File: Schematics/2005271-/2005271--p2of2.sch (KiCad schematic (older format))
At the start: 0 parts

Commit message: Finished up the CAD drawings for 2005271- (AGC module A22).
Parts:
- added G301: Ground-chassis, symbol AGC_DSKY:Ground-chassis
- added J3: ConnectorA1-300, symbol AGC_DSKY:ConnectorA1-300
- added J4: ConnectorA1-400, symbol AGC_DSKY:ConnectorA1-400
- added U201, U203, U205, U209, U211, U213, U214, U216, U218, U221, U224, U225, U227, U229, U231, U233, U235, U237, U239, U243, U245, U246, U248, U250, U252, U256, U258: D3NOR-+4SW-0VDCA-B_C-E_F, symbol D3NOR-+4SW-0VDCA:D3NOR-+4SW-0VDCA-B_C-E_F
- added U202, U204, U206, U208, U210, U212, U215, U217, U219, U222, U223, U226, U228, U230, U232, U234, U236, U238, U240, U242, U244, U247, U249, U251, U253, U255, U257, U259: D3NOR-+4SW-0VDCA-B_C-DFE, symbol D3NOR-+4SW-0VDCA:D3NOR-+4SW-0VDCA-B_C-DFE
- added U207: D3NOR-FAP-0VDCA-expander-ABC-EDF, symbol D3NOR-FAP-0VDCA-expander:D3NOR-FAP-0VDCA-expander-ABC-EDF
- added U220, U241: D3NOR-FAP-0VDCA-expander-ABC-DEF, symbol D3NOR-FAP-0VDCA-expander:D3NOR-FAP-0VDCA-expander-ABC-DEF
- added U254: D3NOR-FAP-0VDCA-expander-BAC-DEF, symbol D3NOR-FAP-0VDCA-expander:D3NOR-FAP-0VDCA-expander-BAC-DEF
- added U260: D3NOR-+4SW-0VDCA-B_C-D_F, symbol D3NOR-+4SW-0VDCA:D3NOR-+4SW-0VDCA-B_C-D_F
- added X301, X302, X303, X304, X311, X312, X313, X314, X315, X316: Node2, symbol AGC_DSKY:Node2
- added X305, X306, X307, X308, X309, X310, X317, X318, X319, X320, X321, X322, X323: ArrowTwiddle, symbol AGC_DSKY:ArrowTwiddle
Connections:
- new net: J3.358, U225.8 (F)
- new net: G301.1, J4.401
- new net: U252.7 (E), X312.1
- new net: U250.7 (E), X311.1
- new net: U248.7 (E), X315.1
- new net: J3.328, U202.2 (C), U204.2 (C), U206.2 (C), U208.2 (C), U210.2 (C), U212.3 (B), U215.2 (C), U217.2 (C), U219.2 (C), U222.2 (C), U223.2 (C), U226.2 (C), U228.2 (C), U230.2 (C)
- new net: U239.7 (E), X313.1
- new net: J4.458, U256.7 (E), X319.1 (pwr)
- new net: J4.453, U253.6 (D)
- new net: J4.457, U255.6 (D)
- new net: J3.314, U206.7 (E)
- new net: U237.7 (E), X316.1
- new net: U235.7 (E), X314.1
- new net: J3.326, U210.7 (E)
- new net: J3.320, U209.8 (F), X309.1 (pwr)
- new net: J4.434, U246.7 (E), X317.1 (pwr)
- new net: J3.342, U212.6 (D), U215.6 (D), U217.6 (D), U219.6 (D), U222.6 (D), U223.6 (D)
- new net: J3.340, U217.7 (E)
- new net: J3.345, U219.7 (E)
- new net: U218.1 (J), U219.3 (B), U219.8 (F)
- new net: U219.9 (K), U220.6 (D)
- new net: U218.3 (B), U219.1 (J)
- new net: J3.334, U201.7 (E), U203.7 (E), U205.7 (E), U209.7 (E), U211.7 (E), U213.7 (E), U214.8 (F), U216.7 (E), U218.7 (E), U221.7 (E), U224.7 (E), U225.7 (E), U227.8 (F), U229.7 (E)
- new net: J3.344, U218.8 (F), X307.1 (pwr)
- new net: U218.2 (C), U218.9 (K)
- new net: J3.330, U212.7 (E)
- new net: J3.337, U216.8 (F), X308.1 (pwr)
- new net: J3.335, U215.7 (E)
- new net: J4.440, U249.6 (D)
- new net: J3.331, U207.1 (J), U207.9 (K), U220.1 (J), U220.9 (K)
- new net: J4.469, U260.6 (D)
- new net: J4.437, U231.7 (E), U233.8 (F), U235.8 (F), U237.8 (F), U239.8 (F), U243.8 (F), U245.8 (F), U246.8 (F), U248.8 (F), U250.8 (F), U252.8 (F), U256.8 (F), U258.8 (F), U260.8 (F)
- new net: U260.2 (C), U260.9 (K)
- new net: U259.3 (B), U259.8 (F), U260.1 (J)
- new net: U259.1 (J), U260.3 (B)
- new net: J4.445, U251.6 (D)
- new net: J3.304, U202.6 (D)
- new net: J4.463, U258.7 (E)
- new net: U258.2 (C), U258.9 (K)
- new net: U257.3 (B), U257.8 (F), U258.1 (J)
- new net: U257.1 (J), U258.3 (B)
- new net: J3.357, U223.7 (E)
- new net: J3.308, U203.8 (F), X310.1 (pwr)
- new net: J3.309, U204.7 (E)
- new net: J3.306, U202.7 (E), U204.6 (D), U206.6 (D), U208.6 (D), U210.6 (D)
- new net: J4.435, U247.6 (D)
- new net: J4.428, U232.2 (C), U234.2 (C), U236.2 (C), U238.2 (C), U240.2 (C), U242.3 (B), U244.2 (C), U247.2 (C), U249.2 (C), U251.2 (C), U253.2 (C), U255.2 (C), U257.2 (C), U259.2 (C)
- new net: J4.430, U244.6 (D)
- new net: J3.303, U201.8 (F)
- new net: J4.432, U245.7 (E), X320.1 (pwr)
- new net: J3.313, U205.8 (F), X305.1 (pwr)
- new net: J4.466, U244.7 (E), U247.7 (E), U249.7 (E), U251.7 (E), U253.7 (E), U255.7 (E), U257.7 (E), U259.6 (D)
- new net: U252.2 (C), U252.9 (K)
- new net: U252.3 (B), U253.1 (J)
- new net: U252.1 (J), U253.3 (B), U253.8 (F)
- new net: U253.9 (K), U254.2 (C)
- new net: U250.1 (J), U251.3 (B), U251.8 (F)
- new net: U250.2 (C), U250.9 (K)
- new net: U250.3 (B), U251.1 (J)
- new net: U251.9 (K), U254.4 (A)
- new net: U255.3 (B), U255.8 (F), U256.1 (J)
- new net: U254.8 (F), U255.9 (K)
- new net: U255.1 (J), U256.3 (B)
- new net: J4.462, U257.6 (D)
- new net: U254.7 (E), U257.9 (K)
- new net: U256.2 (C), U256.9 (K)
- new net: J4.468, U259.7 (E)
- new net: U254.6 (D), U259.9 (K)
- new net: U239.3 (B), U240.1 (J)
- new net: U239.1 (J), U240.3 (B), U240.8 (F)
- new net: J4.427, U243.7 (E), X318.1 (pwr)
- new net: U248.2 (C), U248.9 (K)
- new net: U248.1 (J), U249.3 (B), U249.8 (F)
- new net: U248.3 (B), U249.1 (J)
- new net: U249.9 (K), U254.3 (B)
- new net: J3.319, U208.7 (E)
- new net: J4.419, U240.6 (D)
- new net: J4.408, U232.7 (E), U234.7 (E), U236.7 (E), U238.7 (E), U240.7 (E), U242.6 (D)
- new net: U240.9 (K), U241.6 (D)
- new net: U207.6 (D), U210.9 (K)
- new net: U207.7 (E), U208.9 (K)
- new net: U207.8 (F), U212.9 (K)
- new net: U206.9 (K), U207.2 (C)
- new net: U204.9 (K), U207.3 (B)
- new net: U202.9 (K), U207.4 (A)
- new net: J4.426, U242.7 (E)
- new net: U246.3 (B), U247.1 (J)
- new net: U246.1 (J), U247.3 (B), U247.8 (F)
- new net: J3.352, U221.8 (F), X306.1 (pwr)
- new net: U246.2 (C), U246.9 (K)
- new net: U241.4 (A), U247.9 (K)
- new net: U244.3 (B), U244.8 (F), U245.1 (J)
- new net: U241.3 (B), U244.9 (K)
- new net: U244.1 (J), U245.3 (B)
- new net: U245.2 (C), U245.9 (K)
- new net: U242.2 (C), U242.8 (F), U243.1 (J)
- new net: U241.2 (C), U242.9 (K)
- new net: U242.1 (J), U243.3 (B)
- new net: U243.2 (C), U243.9 (K)
- new net: J3.362, U226.7 (E)
- new net: J3.363, U227.7 (E)
- new net: J3.364, U226.6 (D), U228.6 (D), U230.7 (E)
- new net: J3.365, U228.9 (K)
- new net: J3.366, U228.7 (E)
- new net: J4.414, U238.6 (D)
- new net: J4.431, U241.1 (J), U241.9 (K), U254.1 (J), U254.9 (K)
- new net: J3.369, U229.8 (F)
- new net: U237.3 (B), U238.1 (J)
- new net: U237.1 (J), U238.3 (B), U238.8 (F)
- new net: U238.9 (K), U241.7 (E)
- new net: U239.2 (C), U239.9 (K)
- new net: U229.3 (B), U230.1 (J)
- new net: U229.1 (J), U230.3 (B), U230.8 (F)
- new net: J3.371, U230.6 (D)
- new net: J3.370, U230.9 (K)
- new net: U231.1 (J), U232.3 (B), U232.8 (F)
- new net: U231.2 (C), U231.9 (K)
- new net: U231.3 (B), U232.1 (J)
- new net: J4.402, U231.8 (F)
- new net: J4.405, U232.6 (D)
- new net: J4.403, U232.9 (K)
- new net: U233.1 (J), U234.3 (B), U234.8 (F)
- new net: U233.2 (C), U233.9 (K)
- new net: U233.3 (B), U234.1 (J)
- new net: J4.404, U233.7 (E)
- new net: U229.2 (C), U229.9 (K)
- new net: U224.8 (F), X301.1
- new net: U217.9 (K), U220.7 (E)
- new net: U215.9 (K), U220.8 (F)
- new net: U220.2 (C), U226.9 (K)
- new net: U220.3 (B), U223.9 (K)
- new net: U220.4 (A), U222.9 (K)
- new net: U227.3 (B), U228.1 (J)
- new net: U227.1 (J), U228.3 (B), U228.8 (F)
- new net: U214.7 (E), X302.1
- new net: U213.8 (F), X304.1
- new net: U211.8 (F), X303.1
- new net: J4.406, U234.6 (D)
- new net: J4.409, U236.6 (D)
- new net: U223.1 (J), U224.3 (B)
- new net: U223.3 (B), U223.8 (F), U224.1 (J)
- new net: U221.3 (B), U222.1 (J)
- new net: U221.1 (J), U222.3 (B), U222.8 (F)
- new net: J3.353, U222.7 (E)
- new net: U221.2 (C), U221.9 (K)
- new net: U227.2 (C), U227.9 (K)
- new net: U225.3 (B), U226.1 (J)
- new net: U225.1 (J), U226.3 (B), U226.8 (F)
- new net: U225.2 (C), U225.9 (K)
- new net: U224.2 (C), U224.9 (K)
- new net: U201.1 (J), U202.3 (B), U202.8 (F)
- new net: U201.2 (C), U201.9 (K)
- new net: U201.3 (B), U202.1 (J)
- new net: U212.1 (J), U213.3 (B)
- new net: U212.2 (C), U212.8 (F), U213.1 (J)
- new net: U203.2 (C), U203.9 (K)
- new net: U203.1 (J), U204.3 (B), U204.8 (F)
- new net: U203.3 (B), U204.1 (J)
- new net: U205.1 (J), U206.3 (B), U206.8 (F)
- new net: U205.3 (B), U206.1 (J)
- new net: U205.2 (C), U205.9 (K)
- new net: U208.3 (B), U208.8 (F), U209.1 (J)
- new net: J4.407, U234.9 (K)
- new net: U213.2 (C), U213.9 (K)
- new net: U210.1 (J), U211.3 (B)
- new net: U210.3 (B), U210.8 (F), U211.1 (J)
- new net: U211.2 (C), U211.9 (K)
- new net: U216.1 (J), U217.3 (B), U217.8 (F)
- new net: U216.2 (C), U216.9 (K)
- new net: U216.3 (B), U217.1 (J)
- new net: U214.1 (J), U215.3 (B), U215.8 (F)
- new net: U214.2 (C), U214.9 (K)
- new net: U214.3 (B), U215.1 (J)
- new net: U236.9 (K), U241.8 (F)
- new net: U209.2 (C), U209.9 (K)
- new net: U237.2 (C), U237.9 (K)
- new net: U235.1 (J), U236.3 (B), U236.8 (F)
- new net: U235.3 (B), U236.1 (J)
- new net: U235.2 (C), U235.9 (K)
- new net: U208.1 (J), U209.3 (B)
- new net +4SW: J3.324, J3.348, J4.424, J4.448, U201.10 (+4SW), U202.10 (+4SW), U203.10 (+4SW), U204.10 (+4SW), U205.10 (+4SW), U206.10 (+4SW), U208.10 (+4SW), U209.10 (+4SW), U210.10 (+4SW), U211.10 (+4SW), U212.10 (+4SW), U213.10 (+4SW), U214.10 (+4SW), U215.10 (+4SW), U216.10 (+4SW), U217.10 (+4SW), U218.10 (+4SW), U219.10 (+4SW), U221.10 (+4SW), U222.10 (+4SW), U223.10 (+4SW), U224.10 (+4SW), U225.10 (+4SW), U226.10 (+4SW), U227.10 (+4SW), U228.10 (+4SW), U229.10 (+4SW), U230.10 (+4SW), U231.10 (+4SW), U232.10 (+4SW), U233.10 (+4SW), U234.10 (+4SW), U235.10 (+4SW), U236.10 (+4SW), U237.10 (+4SW), U238.10 (+4SW), U239.10 (+4SW), U240.10 (+4SW), U242.10 (+4SW), U243.10 (+4SW), U244.10 (+4SW), U245.10 (+4SW), U246.10 (+4SW), U247.10 (+4SW), U248.10 (+4SW), U249.10 (+4SW), U250.10 (+4SW), U251.10 (+4SW), U252.10 (+4SW), U253.10 (+4SW), U255.10 (+4SW), U256.10 (+4SW), U257.10 (+4SW), U258.10 (+4SW), U259.10 (+4SW), U260.10 (+4SW), X323.1 (pwr)
- new net 0VDCA: J3.312, J3.336, J3.360, J4.412, J4.436, J4.460, U201.4 (0VDCA), U201.5 (0VDCA), U201.6 (0VDCA), U202.4 (0VDCA), U202.5 (0VDCA), U203.4 (0VDCA), U203.5 (0VDCA), U203.6 (0VDCA), U204.4 (0VDCA), U204.5 (0VDCA), U205.4 (0VDCA), U205.5 (0VDCA), U205.6 (0VDCA), U206.4 (0VDCA), U206.5 (0VDCA), U207.5 (0VDCA), U208.4 (0VDCA), U208.5 (0VDCA), U209.4 (0VDCA), U209.5 (0VDCA), U209.6 (0VDCA), U210.4 (0VDCA), U210.5 (0VDCA), U211.4 (0VDCA), U211.5 (0VDCA), U211.6 (0VDCA), U212.4 (0VDCA), U212.5 (0VDCA), U213.4 (0VDCA), U213.5 (0VDCA), U213.6 (0VDCA), U214.4 (0VDCA), U214.5 (0VDCA), U214.6 (0VDCA), U215.4 (0VDCA), U215.5 (0VDCA), U216.4 (0VDCA), U216.5 (0VDCA), U216.6 (0VDCA), U217.4 (0VDCA), U217.5 (0VDCA), U218.4 (0VDCA), U218.5 (0VDCA), U218.6 (0VDCA), U219.4 (0VDCA), U219.5 (0VDCA), U220.5 (0VDCA), U221.4 (0VDCA), U221.5 (0VDCA), U221.6 (0VDCA), U222.4 (0VDCA), U222.5 (0VDCA), U223.4 (0VDCA), U223.5 (0VDCA), U224.4 (0VDCA), U224.5 (0VDCA), U224.6 (0VDCA), U225.4 (0VDCA), U225.5 (0VDCA), U225.6 (0VDCA), U226.4 (0VDCA), U226.5 (0VDCA), U227.4 (0VDCA), U227.5 (0VDCA), U227.6 (0VDCA), U228.4 (0VDCA), U228.5 (0VDCA), U229.4 (0VDCA), U229.5 (0VDCA), U229.6 (0VDCA), U230.4 (0VDCA), U230.5 (0VDCA), U231.4 (0VDCA), U231.5 (0VDCA), U231.6 (0VDCA), U232.4 (0VDCA), U232.5 (0VDCA), U233.4 (0VDCA), U233.5 (0VDCA), U233.6 (0VDCA), U234.4 (0VDCA), U234.5 (0VDCA), U235.4 (0VDCA), U235.5 (0VDCA), U235.6 (0VDCA), U236.4 (0VDCA), U236.5 (0VDCA), U237.4 (0VDCA), U237.5 (0VDCA), U237.6 (0VDCA), U238.4 (0VDCA), U238.5 (0VDCA), U239.4 (0VDCA), U239.5 (0VDCA), U239.6 (0VDCA), U240.4 (0VDCA), U240.5 (0VDCA), U241.5 (0VDCA), U242.4 (0VDCA), U242.5 (0VDCA), U243.4 (0VDCA), U243.5 (0VDCA), U243.6 (0VDCA), U244.4 (0VDCA), U244.5 (0VDCA), U245.4 (0VDCA), U245.5 (0VDCA), U245.6 (0VDCA), U246.4 (0VDCA), U246.5 (0VDCA), U246.6 (0VDCA), U247.4 (0VDCA), U247.5 (0VDCA), U248.4 (0VDCA), U248.5 (0VDCA), U248.6 (0VDCA), U249.4 (0VDCA), U249.5 (0VDCA), U250.4 (0VDCA), U250.5 (0VDCA), U250.6 (0VDCA), U251.4 (0VDCA), U251.5 (0VDCA), U252.4 (0VDCA), U252.5 (0VDCA), U252.6 (0VDCA), U253.4 (0VDCA), U253.5 (0VDCA), U254.5 (0VDCA), U255.4 (0VDCA), U255.5 (0VDCA), U256.4 (0VDCA), U256.5 (0VDCA), U256.6 (0VDCA), U257.4 (0VDCA), U257.5 (0VDCA), U258.4 (0VDCA), U258.5 (0VDCA), U258.6 (0VDCA), U259.4 (0VDCA), U259.5 (0VDCA), U260.4 (0VDCA), U260.5 (0VDCA), U260.7 (0VDCA), X322.1 (pwr)
- new net FAP: J3.332, U207.10 (FAP), U220.10 (FAP), U241.10 (FAP), U254.10 (FAP), X321.1 (pwr)
- no-connect marks 0 -> 65
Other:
- note added: "SPARE PINS"
- note added: "TO PIN G AND\nUNUSED INPUTS OF\n47300 AND 47400\nSERIES GATES"
- note added: "TO PIN V OF GATES\n47360\n47343\n47321\n47334\n47447\n45460\n47434\n47421"
- note added: "TO PIN V OF \n47300 AND 47400\nSERIES GATES \nEXCEPT THOSE \nGATES TIED TO\nFAP PIN (332)"

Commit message: Finished cross-checking and correcting all 2003200 modules for connector-pad captioning vs Mike's pin DB.  Some discrepancies remain, so it's possible there will be a few upcoming changes related to that, but the default is to assume that the labeling in the drawings is correct and that the differences in the pin DB relate to 2003993.
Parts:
- J3, J4: Caption (none) -> 0VDCA
- J3, J4: Caption (none) -> +4SW
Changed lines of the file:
@@
 F 2 "" H 40375 26900 140 0001 C CNN
 F 3 "" H 40375 26900 140 0001 C CNN
-F 4 "" H 40375 26650 140 0000 C BNB "Caption"
+F 4 "0VDCA" H 40375 26650 140 0001 C BNB "Caption"
 	12   40375 26425
 	1    0    0    -1
@@
 F 2 "" H 36500 27900 140 0001 C CNN
 F 3 "" H 36500 27900 140 0001 C CNN
-F 4 "" H 36500 27650 140 0000 C BNB "Caption"
+F 4 "0VDCA" H 36500 27650 140 0001 C BNB "Caption"
 	60   36500 27425
 	1    0    0    -1
@@
 F 2 "" H 36500 28725 140 0001 C CNN
 F 3 "" H 36500 28725 140 0001 C CNN
-F 4 "" H 36500 28475 140 0000 C BNB "Caption"
+F 4 "+4SW" H 36500 28475 140 0001 C BNB "Caption"
 	24   36500 28250
 	1    0    0    -1
@@
 F 2 "" H 40375 27900 140 0001 C CNN
 F 3 "" H 40375 27900 140 0001 C CNN
-F 4 "" H 40375 27650 140 0000 C BNB "Caption"
+F 4 "0VDCA" H 40375 27650 140 0001 C BNB "Caption"
 	60   40375 27425
 	1    0    0    -1
@@
 F 2 "" H 40375 27400 140 0001 C CNN
 F 3 "" H 40375 27400 140 0001 C CNN
-F 4 "" H 40375 27150 140 0000 C BNB "Caption"
+F 4 "0VDCA" H 40375 27150 140 0001 C BNB "Caption"
 	36   40375 26925
 	1    0    0    -1
@@
 F 2 "" H 40375 29225 140 0001 C CNN
 F 3 "" H 40375 29225 140 0001 C CNN
-F 4 "" H 40375 28975 140 0000 C BNB "Caption"
+F 4 "+4SW" H 40375 28975 140 0001 C BNB "Caption"
 	48   40375 28750
 	1    0    0    -1
@@
 F 2 "" H 40375 28725 140 0001 C CNN
 F 3 "" H 40375 28725 140 0001 C CNN
-F 4 "" H 40375 28475 140 0000 C BNB "Caption"
+F 4 "+4SW" H 40375 28475 140 0001 C BNB "Caption"
 	24   40375 28250
 	1    0    0    -1
@@
 F 2 "" H 36500 26900 140 0001 C CNN
 F 3 "" H 36500 26900 140 0001 C CNN
-F 4 "" H 36500 26650 140 0000 C BNB "Caption"
+F 4 "0VDCA" H 36500 26650 140 0001 C BNB "Caption"
 	12   36500 26425
 	1    0    0    -1

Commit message: Drawing 2005217- now translates to compilable Verilog.
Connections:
- net CHWL12_: now reaches U252.7 (E), X312.1
- net CHWL12_: now also J3.352, U221.8 (F), X306.1 (pwr)
- net CHWL11_: now reaches U250.7 (E), X311.1
- net CHWL11_: now also J3.344, U218.8 (F), X307.1 (pwr)
- net CHWL10_: now reaches U248.7 (E), X315.1
- net CHWL10_: now also J3.337, U216.8 (F), X308.1 (pwr)
- net CHWL06_: now reaches U239.7 (E), X313.1
- net CHWL06_: now also J3.320, U209.8 (F), X309.1 (pwr)
- net CHWL13_: now reaches J4.458, U256.7 (E), X319.1 (pwr)
- net CHWL13_: now also U224.8 (F), X301.1
- net CHWL05_: now reaches U237.7 (E), X316.1
- net CHWL05_: now also J3.313, U205.8 (F), X305.1 (pwr)
- net CHWL04_: now reaches U235.7 (E), X314.1
- net CHWL04_: now also J3.308, U203.8 (F), X310.1 (pwr)
- net CHWL09_: now reaches J4.434, U246.7 (E), X317.1 (pwr)
- net CHWL09_: now also U214.7 (E), X302.1
- net CHWL08_: now reaches J4.432, U245.7 (E), X320.1 (pwr)
- net CHWL08_: now also U213.8 (F), X304.1
- net CHWL07_: now reaches J4.427, U243.7 (E), X318.1 (pwr)
- net CHWL07_: now also U211.8 (F), X303.1

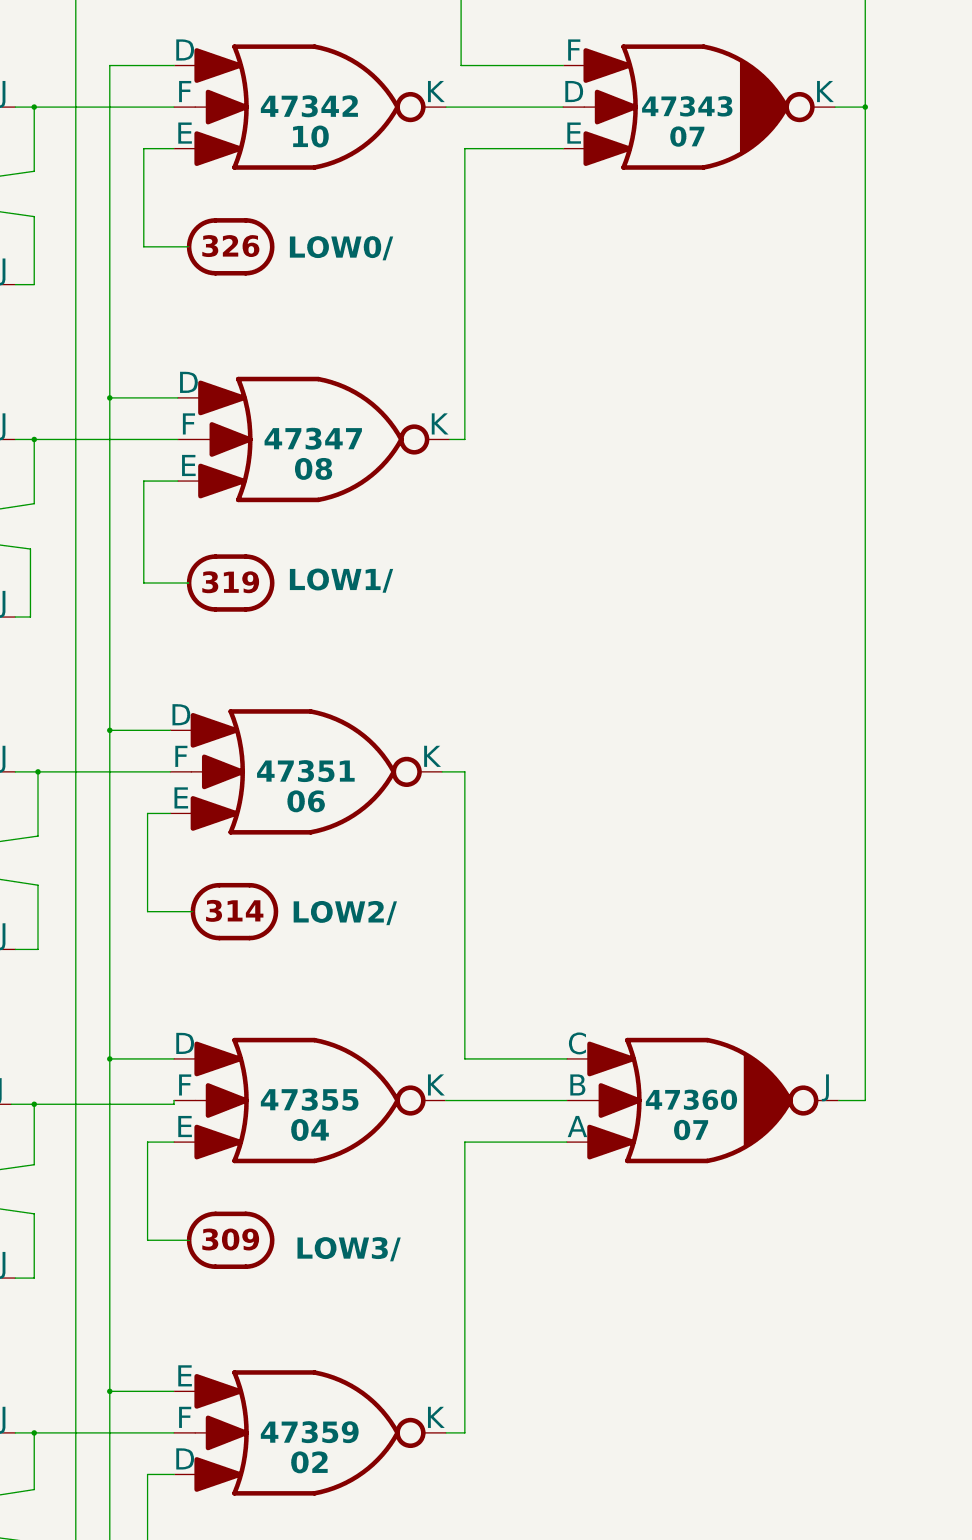
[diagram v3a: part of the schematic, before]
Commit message: Visual fixes made with eelint.  ERC passes. Netlist unchanged.
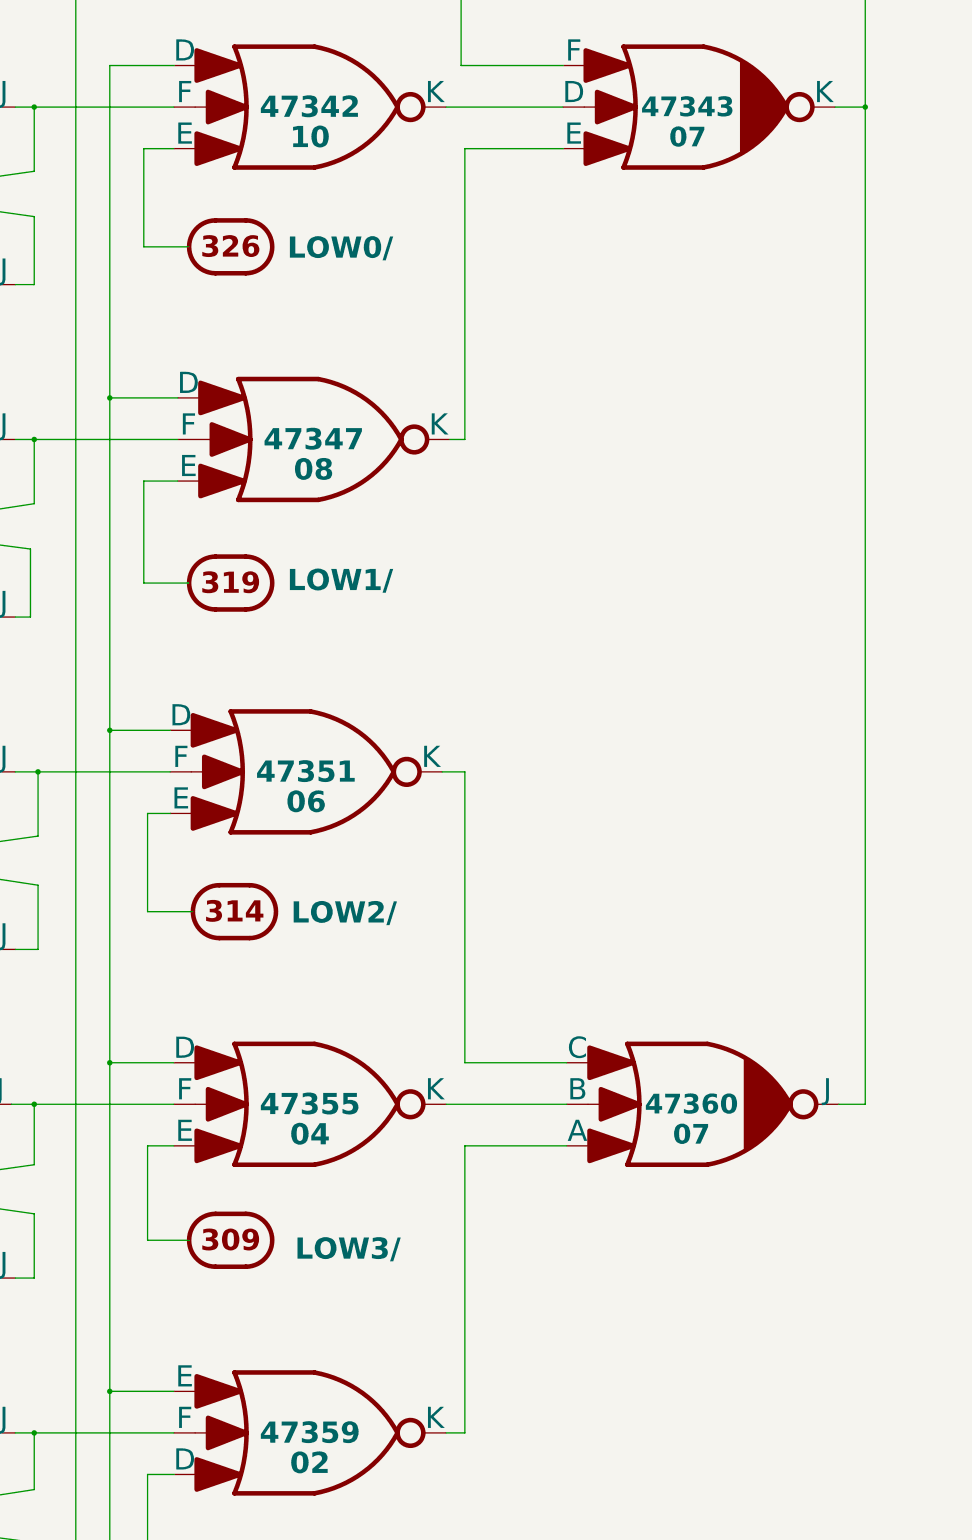
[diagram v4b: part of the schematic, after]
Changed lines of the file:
@@
-EESchema Schematic File Version 4
-LIBS:module-cache
-EELAYER 26 0
+EESchema Schematic File Version 5
+LIBS:errors-cache
+EELAYER 29 0
 EELAYER END
 $Descr E 44000 34000
 encoding utf-8
-Sheet 3 3
+Sheet 1 1
 Title ""
 Date ""
@@
 L D3NOR-+4SW-0VDCA:D3NOR-+4SW-0VDCA-B_C-DFE U204
 U 2 1 66088FAC
-P 9625 28200
-F 0 "U204" H 9625 28525 140 0001 C CNB
-F 1 "D3NOR-+4SW-0VDCA-B_C-DFE" H 9625 28625 140 0001 C CNN
-F 2 "" H 9625 28675 140 0001 C CNN
-F 3 "" H 9625 28675 140 0001 C CNN
-F 4 "47355" H 9625 28200 140 0000 C CNB "Location"
-F 5 "04" H 9625 28000 140 0000 C CNB "Location2"
-	2    9625 28200
+P 9625 28225
+F 0 "U204" H 9625 28550 140 0001 C CNB
+F 1 "D3NOR-+4SW-0VDCA-B_C-DFE" H 9625 28650 140 0001 C CNN
+F 2 "" H 9625 28700 140 0001 C CNN
+F 3 "" H 9625 28700 140 0001 C CNN
+F 4 "47355" H 9625 28225 140 0000 C CNB "Location"
+F 5 "04" H 9625 28025 140 0000 C CNB "Location2"
+	2    9625 28225
 	1    0    0    -1
 $EndComp
@@
 L D3NOR-FAP-0VDCA-expander:D3NOR-FAP-0VDCA-expander-ABC-EDF U207
 U 1 1 66088F45
-P 12225 28200
-F 0 "U207" H 12225 28525 140 0001 C CNB
-F 1 "D3NOR-FAP-0VDCA-expander-ABC-EDF" H 12225 28625 140 0001 C CNN
-F 2 "" H 12225 28675 140 0001 C CNN
-F 3 "" H 12225 28675 140 0001 C CNN
-F 4 "47360" H 12150 28200 130 0000 C CNB "Location"
-F 5 "07" H 12150 28400 130 0000 C CNB "Location2"
-	1    12225 28200
+P 12225 28225
+F 0 "U207" H 12225 28550 140 0001 C CNB
+F 1 "D3NOR-FAP-0VDCA-expander-ABC-EDF" H 12225 28650 140 0001 C CNN
+F 2 "" H 12225 28700 140 0001 C CNN
+F 3 "" H 12225 28700 140 0001 C CNN
+F 4 "47360" H 12150 28225 130 0000 C CNB "Location"
+F 5 "07" H 12150 28425 130 0000 C CNB "Location2"
+	1    12225 28225
 	1    0    0    1
 $EndComp
@@
 	7650 28225 7800 28225
 Wire Wire Line
-	8725 28225 8725 28200
+	7800 28225 8725 28225
 Wire Wire Line
 	5875 31825 5200 31825
@@
 	7800 23825 8750 23825
 Wire Wire Line
-	10525 28200 11325 28200
+	10525 28225 11325 28225
 Wire Wire Line
-	13300 21625 13300 28200
+	13300 21625 13300 28225
 Wire Wire Line
-	13125 28200 13300 28200
+	13125 28225 13300 28225
 Wire Wire Line
 	10500 26025 10650 26025
 Wire Wire Line
-	10650 26025 10650 27925
+	10650 26025 10650 27950
 Wire Wire Line
-	10650 27925 11325 27925
+	10650 27950 11325 27950
 Wire Wire Line
-	11325 28475 10650 28475
+	11325 28500 10650 28500
 Wire Wire Line
-	10650 28475 10650 30400
+	10650 28500 10650 30400
 Wire Wire Line
 	10650 30400 10525 30400
@@
 	8300 23550 8300 25750
 Wire Wire Line
-	8300 25750 8300 27925
+	8300 25750 8300 27950
 Connection ~ 8300 25750
 Wire Wire Line
@@
 Connection ~ 8300 30125
 Wire Wire Line
-	8725 27925 8300 27925
-Connection ~ 8300 27925
+	8725 27950 8300 27950
+Connection ~ 8300 27950
 Wire Wire Line
-	8300 27925 8300 30125
+	8300 27950 8300 30125
 Wire Wire Line
 	8550 26300 8550 26950
@@
 	8550 26300 8700 26300
 Wire Wire Line
-	8725 28475 8550 28475
+	8725 28500 8550 28500
 Wire Wire Line
-	8550 28475 8550 29125
+	8550 28500 8550 29125
 Wire Wire Line
 	8550 29125 8825 29125
@@
 Connection ~ 7800 28225
 Wire Wire Line
-	7800 28225 8725 28225
-Wire Wire Line
 	5850 28500 5700 28500
